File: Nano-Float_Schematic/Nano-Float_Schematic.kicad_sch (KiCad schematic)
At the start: 7 parts, among them M1 Motor_DC, SW1 SW_DIP_x01, U1 MS5837-xxBA

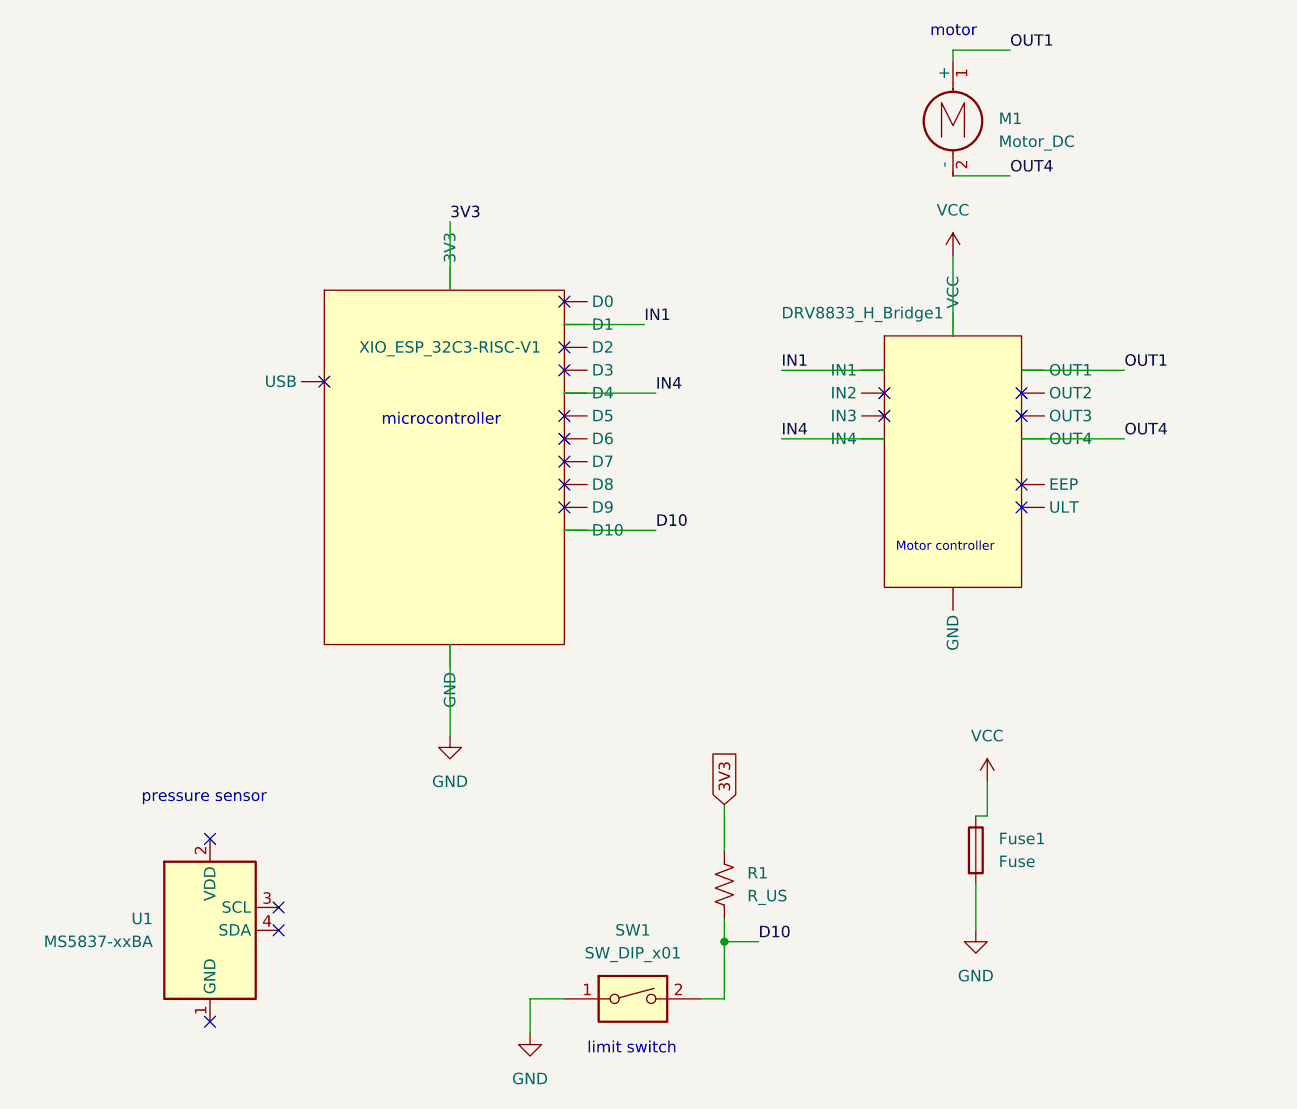
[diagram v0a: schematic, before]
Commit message: Updated Battery Circuit to implement the fuse correctly and added to-do list
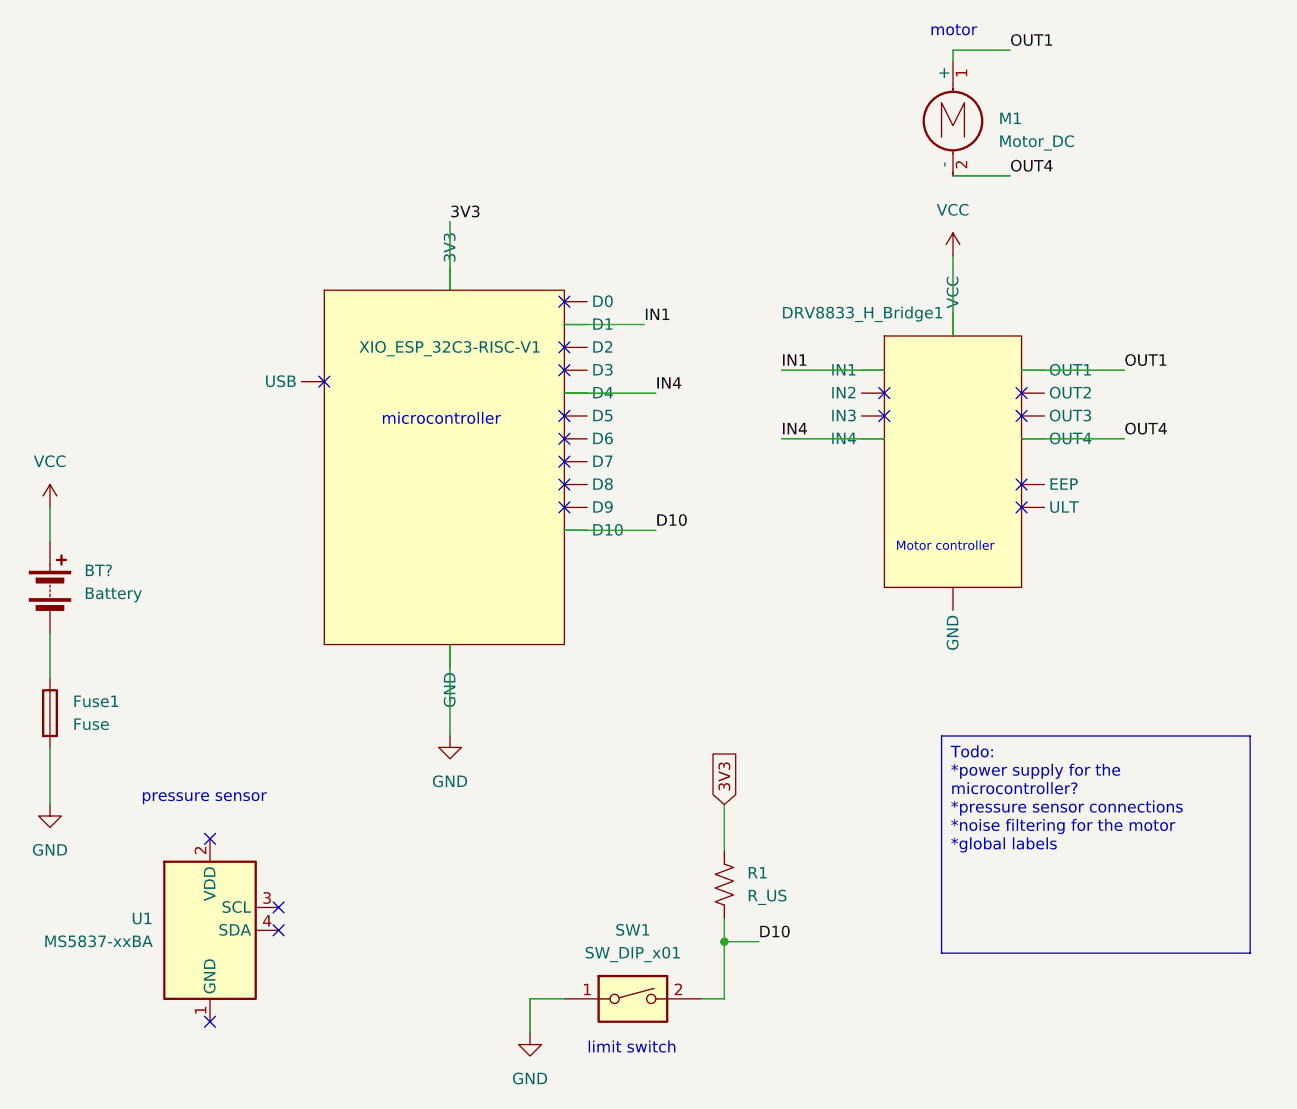
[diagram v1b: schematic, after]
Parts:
- added BT?: Battery, symbol Device:Battery
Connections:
- net VCC: now also BT?.1 (+); no longer Fuse1.1
- new net: BT?.2 (-), Fuse1.1
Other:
- moved on the sheet: Fuse1
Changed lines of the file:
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@@
   (no_connect (at 127 91.44))
   (no_connect (at 162.56 86.36))
-  (wire (pts (xy 172.72 133.35) (xy 173.99 133.35))
-    (stroke (width 0) (type default))
-  )
   (wire (pts (xy 151.13 91.44) (xy 162.56 91.44))
     (stroke (width 0) (type default))
@@
     (stroke (width 0) (type default))
   )
+  (wire (pts (xy 69.85 99.06) (xy 69.85 102.87))
+    (stroke (width 0) (type default))
+  )
+  (wire (pts (xy 170.18 48.26) (xy 176.53 48.26))
+    (stroke (width 0) (type default))
+  )
+  (wire (pts (xy 114.3 67.31) (xy 114.3 74.93))
+    (stroke (width 0) (type default))
+  )
+  (wire (pts (xy 127 78.74) (xy 135.89 78.74))
+    (stroke (width 0) (type default))
+  )
+  (wire (pts (xy 123.19 153.67) (xy 123.19 157.48))
+    (stroke (width 0) (type default))
+  )
+  (wire (pts (xy 170.18 62.23) (xy 176.53 62.23))
+    (stroke (width 0) (type default))
+  )
+  (wire (pts (xy 170.18 71.12) (xy 170.18 80.01))
+    (stroke (width 0) (type default))
+  )
+  (wire (pts (xy 144.78 153.67) (xy 144.78 147.32))
+    (stroke (width 0) (type default))
+  )
+  (wire (pts (xy 69.85 113.03) (xy 69.85 118.11))
+    (stroke (width 0) (type default))
+  )
   (wire (pts (xy 114.3 114.3) (xy 114.3 124.46))
     (stroke (width 0) (type default))
   )
-  (wire (pts (xy 170.18 48.26) (xy 176.53 48.26))
-    (stroke (width 0) (type default))
-  )
-  (wire (pts (xy 172.72 140.97) (xy 172.72 146.05))
-    (stroke (width 0) (type default))
-  )
-  (wire (pts (xy 114.3 67.31) (xy 114.3 74.93))
-    (stroke (width 0) (type default))
-  )
-  (wire (pts (xy 127 78.74) (xy 135.89 78.74))
-    (stroke (width 0) (type default))
-  )
-  (wire (pts (xy 123.19 153.67) (xy 123.19 157.48))
-    (stroke (width 0) (type default))
-  )
-  (wire (pts (xy 170.18 62.23) (xy 176.53 62.23))
-    (stroke (width 0) (type default))
-  )
-  (wire (pts (xy 173.99 133.35) (xy 173.99 129.54))
-    (stroke (width 0) (type default))
-  )
-  (wire (pts (xy 170.18 71.12) (xy 170.18 80.01))
-    (stroke (width 0) (type default))
-  )
-  (wire (pts (xy 144.78 153.67) (xy 144.78 147.32))
-    (stroke (width 0) (type default))
-  )
   (wire (pts (xy 170.18 48.26) (xy 170.18 49.53))
     (stroke (width 0) (type default))
@@
     (stroke (width 0) (type default))
   )
+  (wire (pts (xy 69.85 125.73) (xy 69.85 132.08))
+    (stroke (width 0) (type default))
+  )
   (wire (pts (xy 148.59 147.32) (xy 144.78 147.32))
     (stroke (width 0) (type default))
+  )
+  (text_box "Todo:\n*power supply for the microcontroller?\n*pressure sensor connections\n*noise filtering for the motor\n*global labels\n"
+    (at 168.91 124.46 0) (size 34.29 24.13)
+    (stroke (width 0) (type default))
+    (fill (type none))
+    (effects (font (size 1.27 1.27)) (justify left top))
   )
   (text "Motor controller\n" (at 163.83 104.14 0)
@@
     )
   )
+  (symbol (lib_id "Device:Battery") (at 69.85 107.95 0) (unit 1)
+    (in_bom yes) (on_board yes) (dnp no) (fields_autoplaced)
+    (property "Reference" "BT?" (at 73.66 106.1085 0)
+      (effects (font (size 1.27 1.27)) (justify left))
+    )
+    (property "Value" "Battery" (at 73.66 108.6485 0)
+      (effects (font (size 1.27 1.27)) (justify left))
+    )
+    (property "Footprint" "" (at 69.85 106.426 90)
+      (effects (font (size 1.27 1.27)) hide)
+    )
+    (property "Datasheet" "~" (at 69.85 106.426 90)
+      (effects (font (size 1.27 1.27)) hide)
+    )
+    (pin "1")
+    (pin "2")
+    (instances
+      (project "Nano-Float_Schematic"
+        (path "/f729cb88-08f1-4e9e-8512-18a9fe0c9c6f"
+          (reference "BT?") (unit 1)
+        )
+      )
+    )
+  )
   (symbol (lib_id "Sensor_Pressure:MS5837-xxBA") (at 87.63 146.05 0) (unit 1)
     (in_bom yes) (on_board yes) (dnp no) (fields_autoplaced)
@@
     )
   )
-  (symbol (lib_id "power:GND") (at 172.72 146.05 0) (unit 1)
-    (in_bom yes) (on_board yes) (dnp no) (fields_autoplaced)
-    (property "Reference" "#PWR04" (at 172.72 152.4 0)
-      (effects (font (size 1.27 1.27)) hide)
-    )
-    (property "Value" "GND" (at 172.72 151.13 0)
-      (effects (font (size 1.27 1.27)))
-    )
-    (property "Footprint" "" (at 172.72 146.05 0)
-      (effects (font (size 1.27 1.27)) hide)
-    )
-    (property "Datasheet" "" (at 172.72 146.05 0)
+  (symbol (lib_id "power:GND") (at 69.85 132.08 0) (unit 1)
+    (in_bom yes) (on_board yes) (dnp no) (fields_autoplaced)
+    (property "Reference" "#PWR04" (at 69.85 138.43 0)
+      (effects (font (size 1.27 1.27)) hide)
+    )
+    (property "Value" "GND" (at 69.85 137.16 0)
+      (effects (font (size 1.27 1.27)))
+    )
+    (property "Footprint" "" (at 69.85 132.08 0)
+      (effects (font (size 1.27 1.27)) hide)
+    )
+    (property "Datasheet" "" (at 69.85 132.08 0)
       (effects (font (size 1.27 1.27)) hide)
     )
@@
     )
   )
-  (symbol (lib_id "Device:Fuse") (at 172.72 137.16 0) (unit 1)
-    (in_bom yes) (on_board yes) (dnp no) (fields_autoplaced)
-    (property "Reference" "Fuse1" (at 175.26 135.89 0)
-      (effects (font (size 1.27 1.27)) (justify left))
-    )
-    (property "Value" "Fuse" (at 175.26 138.43 0)
-      (effects (font (size 1.27 1.27)) (justify left))
-    )
-    (property "Footprint" "Fuse:Fuse_0402_1005Metric_Pad0.77x0.64mm_HandSolder" (at 170.942 137.16 90)
-      (effects (font (size 1.27 1.27)) hide)
-    )
-    (property "Datasheet" "~" (at 172.72 137.16 0)
+  (symbol (lib_id "Device:Fuse") (at 69.85 121.92 0) (unit 1)
+    (in_bom yes) (on_board yes) (dnp no) (fields_autoplaced)
+    (property "Reference" "Fuse1" (at 72.39 120.65 0)
+      (effects (font (size 1.27 1.27)) (justify left))
+    )
+    (property "Value" "Fuse" (at 72.39 123.19 0)
+      (effects (font (size 1.27 1.27)) (justify left))
+    )
+    (property "Footprint" "Fuse:Fuse_0402_1005Metric_Pad0.77x0.64mm_HandSolder" (at 68.072 121.92 90)
+      (effects (font (size 1.27 1.27)) hide)
+    )
+    (property "Datasheet" "~" (at 69.85 121.92 0)
       (effects (font (size 1.27 1.27)) hide)
     )
@@
     )
   )
-  (symbol (lib_id "power:VCC") (at 173.99 129.54 0) (unit 1)
-    (in_bom yes) (on_board yes) (dnp no) (fields_autoplaced)
-    (property "Reference" "#PWR05" (at 173.99 133.35 0)
-      (effects (font (size 1.27 1.27)) hide)
-    )
-    (property "Value" "VCC" (at 173.99 124.46 0)
-      (effects (font (size 1.27 1.27)))
-    )
-    (property "Footprint" "" (at 173.99 129.54 0)
-      (effects (font (size 1.27 1.27)) hide)
-    )
-    (property "Datasheet" "" (at 173.99 129.54 0)
-      (effects (font (size 1.27 1.27)) hide)
-    )
+  (symbol (lib_id "power:VCC") (at 69.85 99.06 0) (unit 1)
+    (in_bom yes) (on_board yes) (dnp no) (fields_autoplaced)
+    (property "Reference" "#PWR05" (at 69.85 102.87 0)
+      (effects (font (size 1.27 1.27)) hide)
+    )
+    (property "Value" "VCC" (at 69.85 93.98 0)
+      (effects (font (size 1.27 1.27)))
+    )
+    (property "Footprint" "" (at 69.85 99.06 0)
+      (effects (font (size 1.27 1.27)) hide)
+    )
+    (property "Datasheet" "" (at 69.85 99.06 0)
+      (effects (font (size 1.27 1.27)) hide)
+    )
